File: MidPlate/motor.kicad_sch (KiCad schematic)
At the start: 4 parts, among them J13 JST_BM04B-GHS-TBT, J7 1586842-6

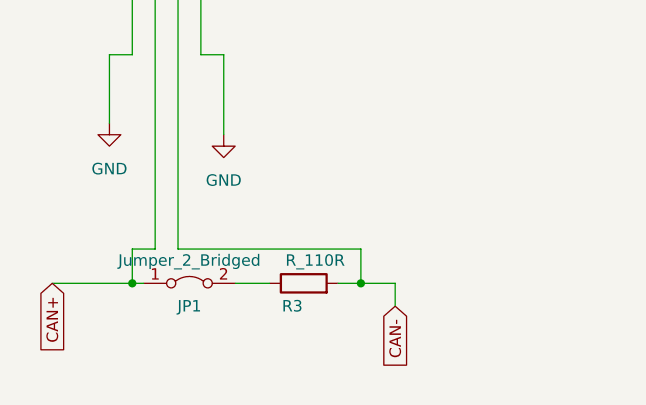
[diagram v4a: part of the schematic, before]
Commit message: update to midplate and powerboard
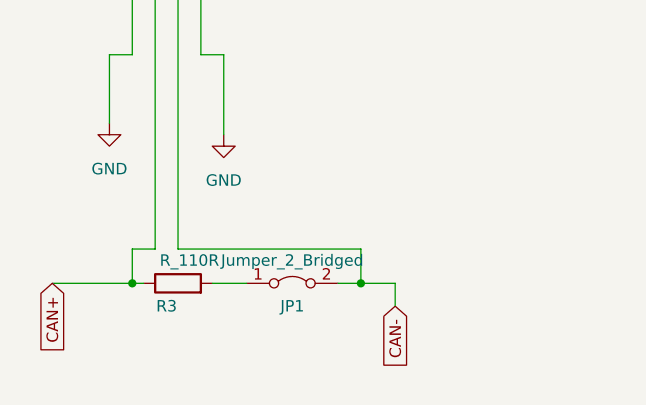
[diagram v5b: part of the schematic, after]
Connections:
- net CAN+: now also R3.1; no longer JP1.1 (A)
- net CAN-: now also JP1.2 (B); no longer R3.2
- new net: JP1.1 (A), R3.2
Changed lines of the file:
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@@
+    (stroke (width 0) (type default))
+  )
+  (wire (pts (xy 119.38 105.41) (xy 123.19 105.41))
     (stroke (width 0) (type default))
   )
@@
   )
   (wire (pts (xy 135.89 101.6) (xy 115.57 101.6))
-    (stroke (width 0) (type default))
-  )
-  (wire (pts (xy 121.92 105.41) (xy 125.73 105.41))
     (stroke (width 0) (type default))
   )
@@
     (property "Intersheetrefs" "${INTERSHEET_REFS}" (at 139.7 116.1967 90)
       (effects (font (size 1.27 1.27)) (justify left) hide)
-    )
-  )
-  (symbol (lib_id "Jumper:Jumper_2_Bridged") (at 116.84 105.41 0) (unit 1)
-    (in_bom yes) (on_board yes) (dnp no)
-    (property "Reference" "JP1" (at 116.84 107.95 0)
-      (effects (font (size 1.27 1.27)))
-    )
-    (property "Value" "Jumper_2_Bridged" (at 116.84 102.87 0)
-      (effects (font (size 1.27 1.27)))
-    )
-    (property "Footprint" "Connector_PinHeader_2.54mm:PinHeader_1x02_P2.54mm_Vertical" (at 116.84 105.41 0)
-      (effects (font (size 1.27 1.27)) hide)
-    )
-    (property "Datasheet" "~" (at 116.84 105.41 0)
-      (effects (font (size 1.27 1.27)) hide)
-    )
-    (pin "1")
-    (pin "2")
-    (instances
-      (project "midplate"
-        (path "/69058343-dac8-421b-a3f6-e069eb1ba8ae/dd4f1e83-2671-4cd9-8990-217fc355ed24"
-          (reference "JP1") (unit 1)
-        )
-        (path "/69058343-dac8-421b-a3f6-e069eb1ba8ae/5956ea5b-5c98-49b4-b8ae-cf424631ffad"
-          (reference "JP1") (unit 1)
-        )
-      )
     )
   )
@@
     )
   )
+  (symbol (lib_id "bots:R_110R") (at 115.57 105.41 90) (unit 1)
+    (in_bom yes) (on_board yes) (dnp no)
+    (property "Reference" "R3" (at 114.3 107.95 90)
+      (effects (font (size 1.27 1.27)))
+    )
+    (property "Value" "R_110R" (at 116.84 102.87 90)
+      (effects (font (size 1.27 1.27)))
+    )
+    (property "Footprint" "bots:R_0603_1608Metric" (at 115.57 107.188 90)
+      (effects (font (size 1.27 1.27)) hide)
+    )
+    (property "Datasheet" "~" (at 115.57 105.41 0)
+      (effects (font (size 1.27 1.27)) hide)
+    )
+    (property "MPN" "0603WAF1100T5E" (at 115.57 105.41 0)
+      (effects (font (size 1.27 1.27)) hide)
+    )
+    (property "Manufacturer" "UNI-ROYAL(Uniroyal Elec)" (at 115.57 105.41 0)
+      (effects (font (size 1.27 1.27)) hide)
+    )
+    (property "Price" "0.001" (at 115.57 105.41 0)
+      (effects (font (size 1.27 1.27)) hide)
+    )
+    (property "JLC" "0603" (at 115.57 105.41 0)
+      (effects (font (size 1.27 1.27)) hide)
+    )
+    (property "LCSC" "C22781" (at 115.57 105.41 0)
+      (effects (font (size 1.27 1.27)) hide)
+    )
+    (pin "1")
+    (pin "2")
+    (instances
+      (project "midplate"
+        (path "/69058343-dac8-421b-a3f6-e069eb1ba8ae/5956ea5b-5c98-49b4-b8ae-cf424631ffad"
+          (reference "R3") (unit 1)
+        )
+      )
+    )
+  )
   (symbol (lib_id "power:GND") (at 107.95 87.63 0) (unit 1)
     (in_bom yes) (on_board yes) (dnp no) (fields_autoplaced)
@@
     )
   )
+  (symbol (lib_id "Jumper:Jumper_2_Bridged") (at 128.27 105.41 0) (unit 1)
+    (in_bom yes) (on_board yes) (dnp no)
+    (property "Reference" "JP1" (at 128.27 107.95 0)
+      (effects (font (size 1.27 1.27)))
+    )
+    (property "Value" "Jumper_2_Bridged" (at 128.27 102.87 0)
+      (effects (font (size 1.27 1.27)))
+    )
+    (property "Footprint" "Connector_PinHeader_2.54mm:PinHeader_1x02_P2.54mm_Vertical" (at 128.27 105.41 0)
+      (effects (font (size 1.27 1.27)) hide)
+    )
+    (property "Datasheet" "~" (at 128.27 105.41 0)
+      (effects (font (size 1.27 1.27)) hide)
+    )
+    (pin "1")
+    (pin "2")
+    (instances
+      (project "midplate"
+        (path "/69058343-dac8-421b-a3f6-e069eb1ba8ae/dd4f1e83-2671-4cd9-8990-217fc355ed24"
+          (reference "JP1") (unit 1)
+        )
+        (path "/69058343-dac8-421b-a3f6-e069eb1ba8ae/5956ea5b-5c98-49b4-b8ae-cf424631ffad"
+          (reference "JP1") (unit 1)
+        )
+      )
+    )
+  )
   (symbol (lib_id "power:GND") (at 170.18 73.66 0) (unit 1)
     (in_bom yes) (on_board yes) (dnp no) (fields_autoplaced)
@@
         )
       )
-    )
-  )
-  (symbol (lib_id "bots:R_110R") (at 129.54 105.41 90) (unit 1)
-    (in_bom yes) (on_board yes) (dnp no)
-    (property "Reference" "R3" (at 128.27 107.95 90)
-      (effects (font (size 1.27 1.27)))
-    )
-    (property "Value" "R_110R" (at 130.81 102.87 90)
-      (effects (font (size 1.27 1.27)))
-    )
-    (property "Footprint" "bots:R_0603_1608Metric" (at 129.54 107.188 90)
-      (effects (font (size 1.27 1.27)) hide)
-    )
-    (property "Datasheet" "~" (at 129.54 105.41 0)
-      (effects (font (size 1.27 1.27)) hide)
-    )
-    (property "MPN" "0603WAF1100T5E" (at 129.54 105.41 0)
-      (effects (font (size 1.27 1.27)) hide)
-    )
-    (property "Manufacturer" "UNI-ROYAL(Uniroyal Elec)" (at 129.54 105.41 0)
-      (effects (font (size 1.27 1.27)) hide)
-    )
-    (property "Price" "0.001" (at 129.54 105.41 0)
-      (effects (font (size 1.27 1.27)) hide)
-    )
-    (property "JLC" "0603" (at 129.54 105.41 0)
-      (effects (font (size 1.27 1.27)) hide)
-    )
-    (property "LCSC" "C22781" (at 129.54 105.41 0)
-      (effects (font (size 1.27 1.27)) hide)
-    )
-    (pin "1")
-    (pin "2")
-    (instances
-      (project "midplate"
-        (path "/69058343-dac8-421b-a3f6-e069eb1ba8ae/5956ea5b-5c98-49b4-b8ae-cf424631ffad"
-          (reference "R3") (unit 1)
-        )
-      )

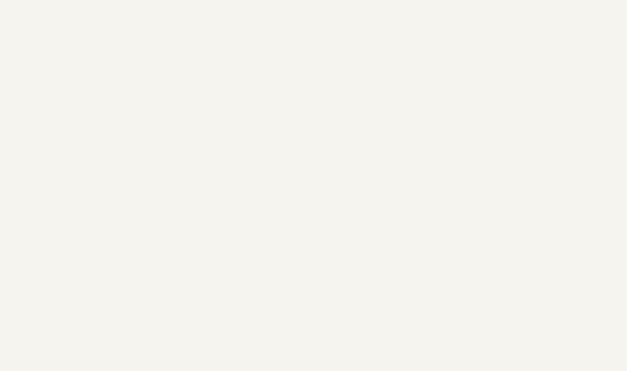
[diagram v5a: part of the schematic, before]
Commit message: power board and midplate updates (mostly finalized)
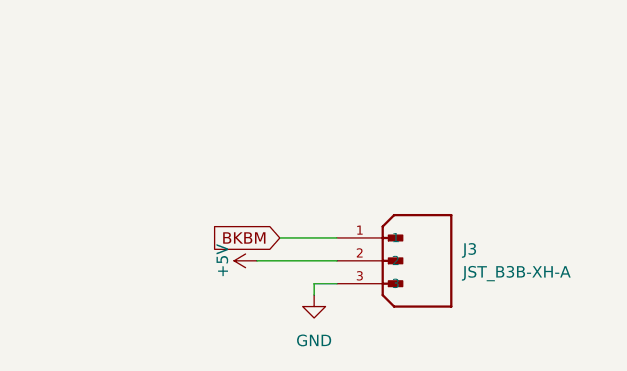
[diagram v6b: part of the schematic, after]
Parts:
- added J3: JST_B3B-XH-A, bots:JST_B3B-XH-A, symbol bots:JST_B3B-XH-A
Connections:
- net GND: now also J3.3
- new net +5V: J3.2
- new net BKBM: J3.1
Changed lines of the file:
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@@
+    (stroke (width 0) (type default))
+  )
+  (wire (pts (xy 179.07 114.3) (xy 185.42 114.3))
+    (stroke (width 0) (type default))
+  )
+  (wire (pts (xy 182.88 119.38) (xy 182.88 120.65))
     (stroke (width 0) (type default))
   )
@@
     (stroke (width 0) (type default))
   )
+  (wire (pts (xy 182.88 119.38) (xy 185.42 119.38))
+    (stroke (width 0) (type default))
+  )
   (wire (pts (xy 120.65 80.01) (xy 120.65 88.9))
     (stroke (width 0) (type default))
@@
   )
   (wire (pts (xy 135.89 105.41) (xy 133.35 105.41))
+    (stroke (width 0) (type default))
+  )
+  (wire (pts (xy 176.53 116.84) (xy 185.42 116.84))
     (stroke (width 0) (type default))
   )
@@
   (label "MP1_POWER" (at 182.88 81.28 0) (fields_autoplaced)
     (effects (font (size 1.27 1.27)) (justify left bottom))
+  )
+  (global_label "BKBM" (shape input) (at 179.07 114.3 180) (fields_autoplaced)
+    (effects (font (size 1.27 1.27)) (justify right))
+    (property "Intersheetrefs" "${INTERSHEET_REFS}" (at 170.8234 114.3 0)
+      (effects (font (size 1.27 1.27)) (justify right) hide)
+    )
   )
   (global_label "CAN+" (shape input) (at 101.6 105.41 270) (fields_autoplaced)
@@
     (property "Intersheetrefs" "${INTERSHEET_REFS}" (at 139.7 116.1967 90)
       (effects (font (size 1.27 1.27)) (justify left) hide)
+    )
+  )
+  (symbol (lib_id "power:+5V") (at 176.53 116.84 90) (unit 1)
+    (in_bom yes) (on_board yes) (dnp no)
+    (property "Reference" "#PWR013" (at 180.34 116.84 0)
+      (effects (font (size 1.27 1.27)) hide)
+    )
+    (property "Value" "+5V" (at 172.72 116.84 0)
+      (effects (font (size 1.27 1.27)))
+    )
+    (property "Footprint" "" (at 176.53 116.84 0)
+      (effects (font (size 1.27 1.27)) hide)
+    )
+    (property "Datasheet" "" (at 176.53 116.84 0)
+      (effects (font (size 1.27 1.27)) hide)
+    )
+    (pin "1")
+    (instances
+      (project "midplate"
+        (path "/69058343-dac8-421b-a3f6-e069eb1ba8ae/ab54f000-c596-4ae0-81be-92723dd47fdf"
+          (reference "#PWR013") (unit 1)
+        )
+        (path "/69058343-dac8-421b-a3f6-e069eb1ba8ae/5699b499-0901-4542-927f-3a0270375bb5"
+          (reference "#PWR020") (unit 1)
+        )
+        (path "/69058343-dac8-421b-a3f6-e069eb1ba8ae/5956ea5b-5c98-49b4-b8ae-cf424631ffad"
+          (reference "#PWR019") (unit 1)
+        )
+      )
+      (project "FacePlate"
+        (path "/e63e39d7-6ac0-4ffd-8aa3-1841a4541b55"
+          (reference "#PWR043") (unit 1)
+        )
+      )
     )
   )
@@
     )
   )
+  (symbol (lib_id "bots:JST_B3B-XH-A") (at 190.5 116.84 0) (unit 1)
+    (in_bom yes) (on_board yes) (dnp no) (fields_autoplaced)
+    (property "Reference" "J3" (at 199.39 115.57 0)
+      (effects (font (size 1.27 1.27)) (justify left))
+    )
+    (property "Value" "JST_B3B-XH-A" (at 199.39 118.11 0)
+      (effects (font (size 1.27 1.27)) (justify left))
+    )
+    (property "Footprint" "bots:JST_B3B-XH-A" (at 190.5 116.84 0)
+      (effects (font (size 1.27 1.27)) (justify bottom) hide)
+    )
+    (property "Datasheet" "" (at 190.5 116.84 0)
+      (effects (font (size 1.27 1.27)) hide)
+    )
+    (property "MPN" "B3B-XH-A(LF)(SN)" (at 190.5 116.84 0)
+      (effects (font (size 1.27 1.27)) (justify bottom) hide)
+    )
+    (property "Manufacturer" "JST Sales America Inc." (at 190.5 116.84 0)
+      (effects (font (size 1.27 1.27)) (justify bottom) hide)
+    )
+    (property "Price" "0.31" (at 190.5 116.84 0)
+      (effects (font (size 1.27 1.27)) hide)
+    )
+    (property "JLC" "" (at 190.5 116.84 0)
+      (effects (font (size 1.27 1.27)) hide)
+    )
+    (property "LCSC" "" (at 190.5 116.84 0)
+      (effects (font (size 1.27 1.27)) hide)
+    )
+    (pin "1")
+    (pin "2")
+    (pin "3")
+    (instances
+      (project "midplate"
+        (path "/69058343-dac8-421b-a3f6-e069eb1ba8ae/5956ea5b-5c98-49b4-b8ae-cf424631ffad"
+          (reference "J3") (unit 1)
+        )
+      )
+    )
+  )
   (symbol (lib_id "power:VCC") (at 195.58 60.96 0) (unit 1)
     (in_bom yes) (on_board yes) (dnp no) (fields_autoplaced)
@@
         )
       )
+    )
+  )
+  (symbol (lib_id "power:GND") (at 182.88 120.65 0) (unit 1)
+    (in_bom yes) (on_board yes) (dnp no) (fields_autoplaced)
+    (property "Reference" "#PWR037" (at 182.88 127 0)
+      (effects (font (size 1.27 1.27)) hide)
+    )
+    (property "Value" "GND" (at 182.88 125.73 0)
+      (effects (font (size 1.27 1.27)))
+    )
+    (property "Footprint" "" (at 182.88 120.65 0)
+      (effects (font (size 1.27 1.27)) hide)
+    )
+    (property "Datasheet" "" (at 182.88 120.65 0)
+      (effects (font (size 1.27 1.27)) hide)
+    )
+    (pin "1")
+    (instances
+      (project "midplate"
+        (path "/69058343-dac8-421b-a3f6-e069eb1ba8ae/ab54f000-c596-4ae0-81be-92723dd47fdf"
+          (reference "#PWR037") (unit 1)
+        )
+        (path "/69058343-dac8-421b-a3f6-e069eb1ba8ae/5699b499-0901-4542-927f-3a0270375bb5"
+          (reference "#PWR05") (unit 1)
+        )
+        (path "/69058343-dac8-421b-a3f6-e069eb1ba8ae/5956ea5b-5c98-49b4-b8ae-cf424631ffad"
+          (reference "#PWR021") (unit 1)
+        )
+      )

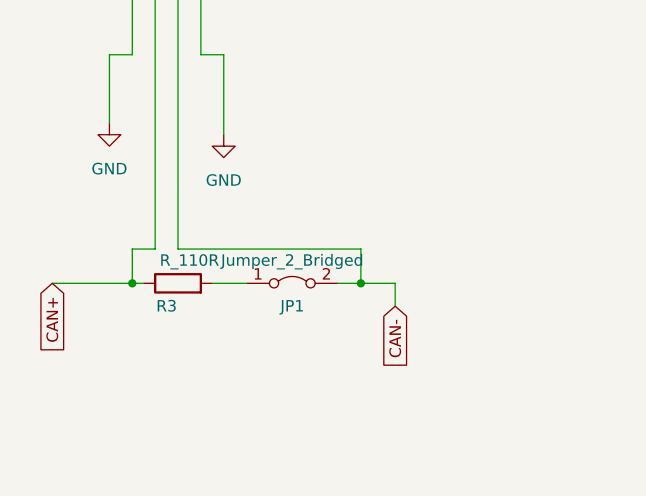
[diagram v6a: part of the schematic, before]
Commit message: midplate 4 layers, chicker shell off limit switch idea
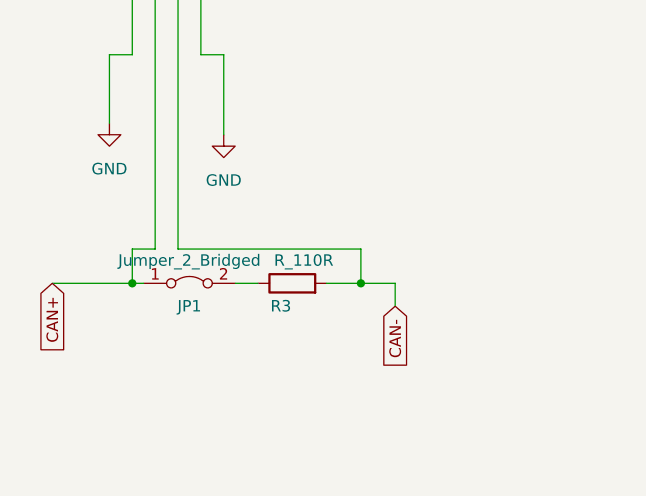
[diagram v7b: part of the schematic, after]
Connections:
- net CAN+: now also JP1.1 (A); no longer R3.1
- net CAN-: now also R3.2; no longer JP1.2 (B)
- new net: JP1.2 (B), R3.1
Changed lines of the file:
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@@
-    (stroke (width 0) (type default))
-  )
-  (wire (pts (xy 119.38 105.41) (xy 123.19 105.41))
     (stroke (width 0) (type default))
   )
@@
     (stroke (width 0) (type default))
   )
+  (wire (pts (xy 121.92 105.41) (xy 124.46 105.41))
+    (stroke (width 0) (type default))
+  )
   (wire (pts (xy 113.03 72.39) (xy 113.03 101.6))
     (stroke (width 0) (type default))
@@
     (stroke (width 0) (type default))
   )
-  (wire (pts (xy 135.89 105.41) (xy 133.35 105.41))
+  (wire (pts (xy 132.08 105.41) (xy 135.89 105.41))
     (stroke (width 0) (type default))
   )
@@
     )
   )
-  (symbol (lib_id "bots:R_110R") (at 115.57 105.41 90) (unit 1)
-    (in_bom yes) (on_board yes) (dnp no)
-    (property "Reference" "R3" (at 114.3 107.95 90)
-      (effects (font (size 1.27 1.27)))
-    )
-    (property "Value" "R_110R" (at 116.84 102.87 90)
-      (effects (font (size 1.27 1.27)))
-    )
-    (property "Footprint" "bots:R_0603_1608Metric" (at 115.57 107.188 90)
-      (effects (font (size 1.27 1.27)) hide)
-    )
-    (property "Datasheet" "~" (at 115.57 105.41 0)
-      (effects (font (size 1.27 1.27)) hide)
-    )
-    (property "MPN" "0603WAF1100T5E" (at 115.57 105.41 0)
-      (effects (font (size 1.27 1.27)) hide)
-    )
-    (property "Manufacturer" "UNI-ROYAL(Uniroyal Elec)" (at 115.57 105.41 0)
-      (effects (font (size 1.27 1.27)) hide)
-    )
-    (property "Price" "0.001" (at 115.57 105.41 0)
-      (effects (font (size 1.27 1.27)) hide)
-    )
-    (property "JLC" "0603" (at 115.57 105.41 0)
-      (effects (font (size 1.27 1.27)) hide)
-    )
-    (property "LCSC" "C22781" (at 115.57 105.41 0)
+  (symbol (lib_id "Jumper:Jumper_2_Bridged") (at 116.84 105.41 0) (unit 1)
+    (in_bom yes) (on_board yes) (dnp no)
+    (property "Reference" "JP1" (at 116.84 107.95 0)
+      (effects (font (size 1.27 1.27)))
+    )
+    (property "Value" "Jumper_2_Bridged" (at 116.84 102.87 0)
+      (effects (font (size 1.27 1.27)))
+    )
+    (property "Footprint" "Connector_PinHeader_2.54mm:PinHeader_1x02_P2.54mm_Vertical" (at 116.84 105.41 0)
+      (effects (font (size 1.27 1.27)) hide)
+    )
+    (property "Datasheet" "~" (at 116.84 105.41 0)
       (effects (font (size 1.27 1.27)) hide)
     )
@@
     (instances
       (project "midplate"
-        (path "/69058343-dac8-421b-a3f6-e069eb1ba8ae/5956ea5b-5c98-49b4-b8ae-cf424631ffad"
-          (reference "R3") (unit 1)
+        (path "/69058343-dac8-421b-a3f6-e069eb1ba8ae/dd4f1e83-2671-4cd9-8990-217fc355ed24"
+          (reference "JP1") (unit 1)
+        )
+        (path "/69058343-dac8-421b-a3f6-e069eb1ba8ae/5956ea5b-5c98-49b4-b8ae-cf424631ffad"
+          (reference "JP1") (unit 1)
         )
       )
@@
     )
   )
-  (symbol (lib_id "Jumper:Jumper_2_Bridged") (at 128.27 105.41 0) (unit 1)
-    (in_bom yes) (on_board yes) (dnp no)
-    (property "Reference" "JP1" (at 128.27 107.95 0)
-      (effects (font (size 1.27 1.27)))
-    )
-    (property "Value" "Jumper_2_Bridged" (at 128.27 102.87 0)
-      (effects (font (size 1.27 1.27)))
-    )
-    (property "Footprint" "Connector_PinHeader_2.54mm:PinHeader_1x02_P2.54mm_Vertical" (at 128.27 105.41 0)
+  (symbol (lib_id "bots:R_110R") (at 128.27 105.41 90) (unit 1)
+    (in_bom yes) (on_board yes) (dnp no)
+    (property "Reference" "R3" (at 127 107.95 90)
+      (effects (font (size 1.27 1.27)))
+    )
+    (property "Value" "R_110R" (at 129.54 102.87 90)
+      (effects (font (size 1.27 1.27)))
+    )
+    (property "Footprint" "bots:R_0603_1608Metric" (at 128.27 107.188 90)
       (effects (font (size 1.27 1.27)) hide)
     )
@@
       (effects (font (size 1.27 1.27)) hide)
     )
+    (property "MPN" "0603WAF1100T5E" (at 128.27 105.41 0)
+      (effects (font (size 1.27 1.27)) hide)
+    )
+    (property "Manufacturer" "UNI-ROYAL(Uniroyal Elec)" (at 128.27 105.41 0)
+      (effects (font (size 1.27 1.27)) hide)
+    )
+    (property "Price" "0.001" (at 128.27 105.41 0)
+      (effects (font (size 1.27 1.27)) hide)
+    )
+    (property "JLC" "0603" (at 128.27 105.41 0)
+      (effects (font (size 1.27 1.27)) hide)
+    )
+    (property "LCSC" "C22781" (at 128.27 105.41 0)
+      (effects (font (size 1.27 1.27)) hide)
+    )
     (pin "1")
     (pin "2")
     (instances
       (project "midplate"
-        (path "/69058343-dac8-421b-a3f6-e069eb1ba8ae/dd4f1e83-2671-4cd9-8990-217fc355ed24"
-          (reference "JP1") (unit 1)
-        )
-        (path "/69058343-dac8-421b-a3f6-e069eb1ba8ae/5956ea5b-5c98-49b4-b8ae-cf424631ffad"
-          (reference "JP1") (unit 1)
-        )
-      )
+        (path "/69058343-dac8-421b-a3f6-e069eb1ba8ae/5956ea5b-5c98-49b4-b8ae-cf424631ffad"
+          (reference "R3") (unit 1)
+        )
+      )
